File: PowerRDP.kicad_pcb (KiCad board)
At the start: 2 copper layers, 72.6 x 36.1 mm, 46 parts, among them J1 Conn_01x02_Male, J10 FPGA, J11 FAA LED, J12 Switch, J2 Conn_01x02_Male, J3 Conn_01x02_Male, J4 Conn_01x02_Male, J5 Conn_01x02_Male, J6 Conn_01x02_Male, J7 3.3V, J8 5V, J9 12V, Q1 NTR4003NT1G, U1 Recom_RS3, U2 LM2575-3.3BU, U3 LM2575-5.0BU, U4 LM2575-12BU, U5 TS555

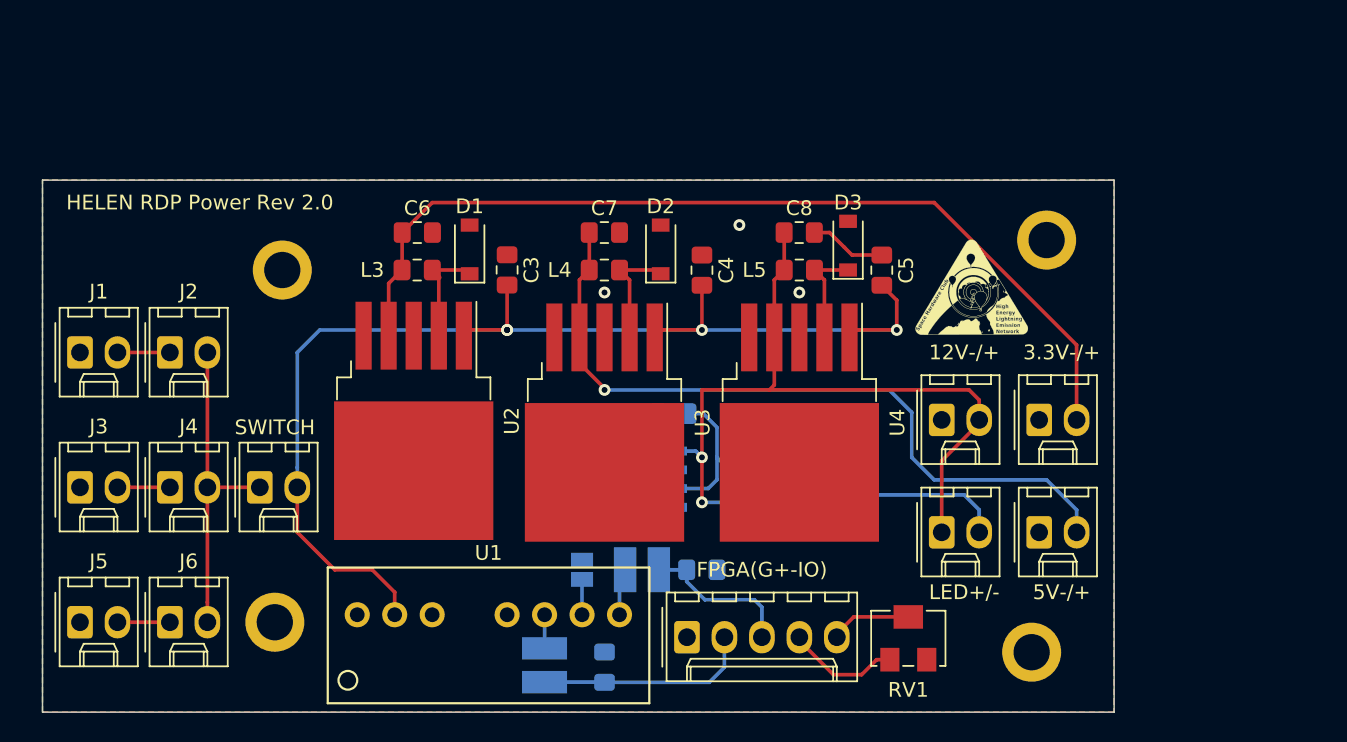
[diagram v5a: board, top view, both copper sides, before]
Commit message: Fix capcaitors and inductors and expand board to sustain girth of new components.
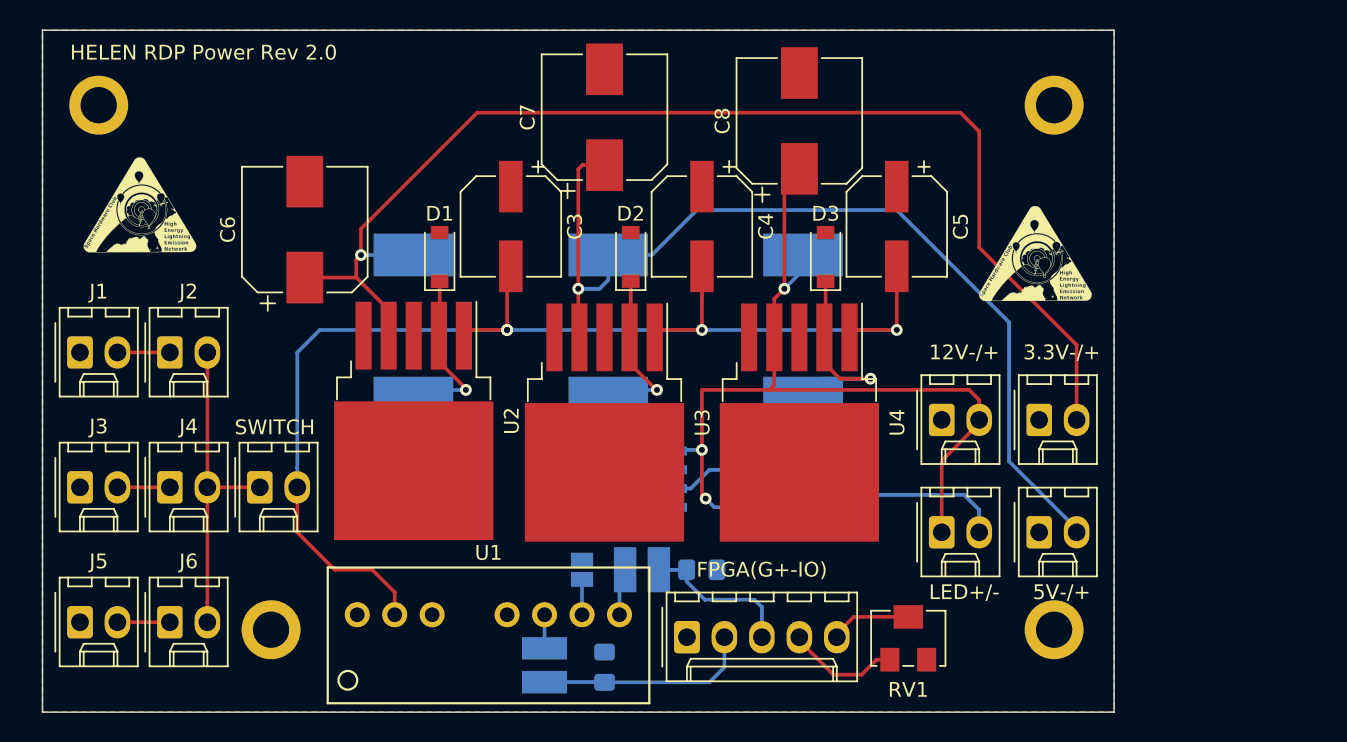
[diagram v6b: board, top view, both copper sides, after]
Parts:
- removed the REF** at (99.6, 85.9)
- removed the REF** at (100.1, 62.0)
- removed the REF** at (151.9, 59.9)
- removed the REF** at (150.9, 87.9)
- added G***: LOGO, rdplibs:HELENlogo_large, F.Cu at (90.4, 57.4)
- added REF**: ScrewHole, rdplibs:ScrewHole, F.Cu at (152.4, 86.4)
- added REF**: ScrewHole, rdplibs:ScrewHole, F.Cu at (99.3, 86.4)
- added REF**: ScrewHole, rdplibs:ScrewHole, F.Cu at (87.6, 50.8)
- added REF**: ScrewHole, rdplibs:ScrewHole, F.Cu at (152.4, 50.8)
- C3, C4, C5: footprint Capacitor_SMD:C_0805_2012Metric_Pad1.15x1.40mm_HandSolder -> Capacitor_SMD:CP_Elec_6.3x7.7
- C6, C7, C8: footprint Capacitor_SMD:C_0805_2012Metric_Pad1.15x1.40mm_HandSolder -> Capacitor_SMD:CP_Elec_8x10
- L3, L4, L5: value 330uH -> 470uH; footprint Inductor_SMD:L_0805_2012Metric_Pad1.15x1.40mm_HandSolder -> Inductor_SMD:L_Bourns_SRR1260; moved to B.Cu
- moved C10 8.98 mm to (120.4, 78.2), turned to 270 degrees
- moved C7 7.82 mm to (121.9, 51.6), turned to 90 degrees
- moved C6 7.63 mm to (101.6, 59.2), turned to 90 degrees
- moved C8 7.57 mm to (135.1, 51.9), turned to 90 degrees
- moved G*** 4.89 mm to (151.1, 60.7)
- moved L4 3.84 mm to (122.2, 65.8), turned to 90 degrees
- moved L5 3.84 mm to (135.4, 65.8), turned to 90 degrees
- moved L3 3.84 mm to (109.0, 65.8), turned to 90 degrees
- moved C5 3.13 mm to (141.7, 59.0)
- moved C4 2.96 mm to (128.5, 59.0)
- moved C3 2.96 mm to (115.6, 59.0)
- moved D2 2.09 mm to (123.7, 61.1)
- moved D1 2.09 mm to (110.7, 61.1)
- moved D3 1.70 mm to (136.9, 61.1)
- moved Q1 0.20 mm to (137.0, 76.6)
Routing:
- net /+3.3V: track 63.0 -> 83.3 mm, vias 0 -> 1
- net /+5V: track 50.3 -> 66.8 mm
- net /+12V: track 63.4 -> 71.5 mm, vias 2 -> 3
- net Net-(D3-Pad1): track 7.12 -> 14.3 mm, vias 0 -> 1
- net GND: track 5.20 -> 0.00 mm, vias 3 -> 0
- net Net-(D2-Pad1): track 7.75 -> 11.7 mm, vias 0 -> 1
- net Net-(D1-Pad1): track 7.99 -> 11.9 mm, vias 0 -> 1
- net /POWR: track 82.7 -> 86.2 mm
- net /THR: track 15.3 -> 12.5 mm
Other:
- board size 72.6 x 36.1 mm -> 72.6 x 46.2 mm
